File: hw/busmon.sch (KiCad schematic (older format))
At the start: 24 parts, among them J1 CONN_01X16, J3 DIL14, J4 DIL14, J5 DIL14, J6 DIL14, J7 CONN_01X02, J8 CONN_01X06, Q1 MMBT3906, Q2 MMBT3906, Q3 MMBT3906, Q4 MMBT3906, U1 ATMEGA164A-A

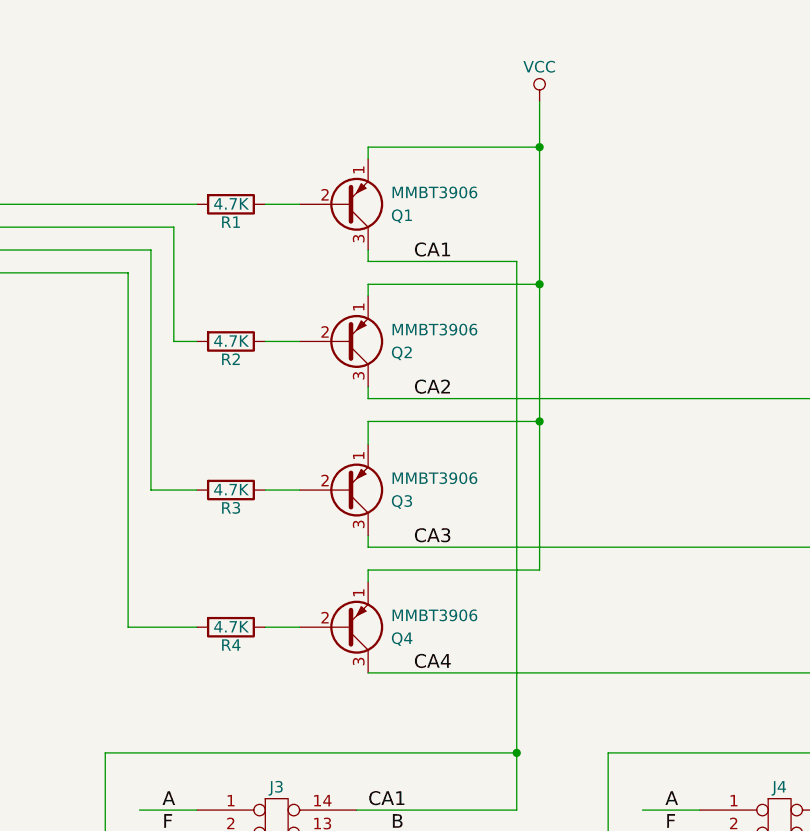
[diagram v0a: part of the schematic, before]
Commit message: use correct transistor pinout
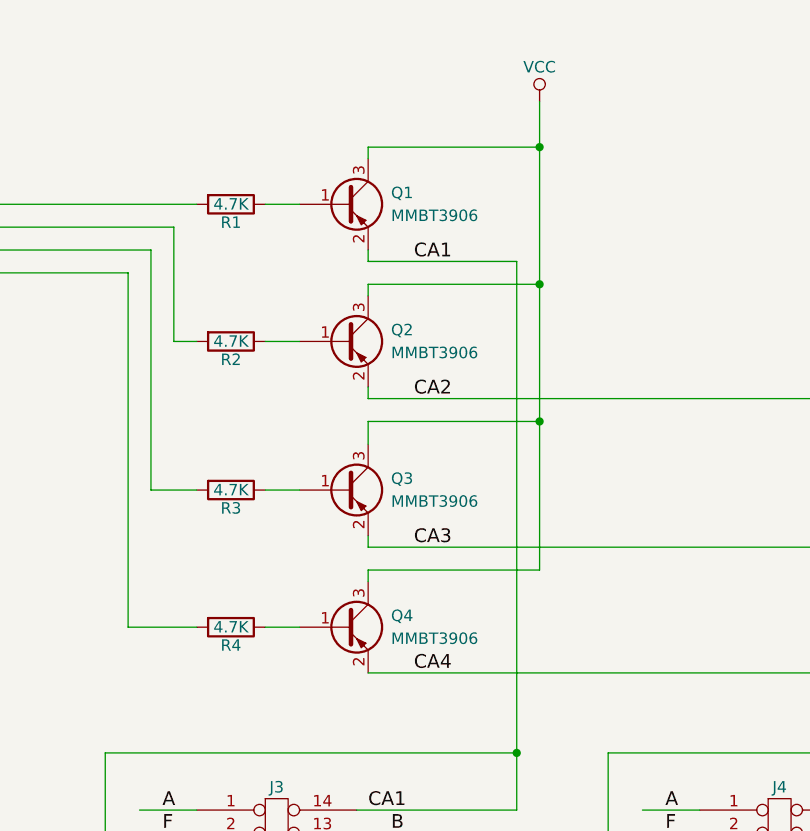
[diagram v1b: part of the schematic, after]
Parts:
- removed Q1, Q2, Q3, Q4: MMBT3906, TO_SOT_Packages_SMD:SOT-23, symbol Q_PNP_EBC
- added Q1, Q2, Q3, Q4: MMBT3906, symbol Q_PNP_BEC
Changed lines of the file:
@@
 CA2
-$Comp
-L Q_PNP_EBC Q1
-U 1 1 592DFC6D
-P 7950 3450
-F 0 "Q1" H 8150 3500 50  0000 L CNN
-F 1 "MMBT3906" H 8150 3400 50  0000 L CNN
-F 2 "TO_SOT_Packages_SMD:SOT-23" H 8150 3550 50  0001 C CNN
-F 3 "" H 7950 3450 50  0001 C CNN
-	1    7950 3450
-	1    0    0    1
-$EndComp
-$Comp
-L Q_PNP_EBC Q2
-U 1 1 592DFCA0
-P 7950 4050
-F 0 "Q2" H 8150 4100 50  0000 L CNN
-F 1 "MMBT3906" H 8150 4000 50  0000 L CNN
-F 2 "TO_SOT_Packages_SMD:SOT-23" H 8150 4150 50  0001 C CNN
-F 3 "" H 7950 4050 50  0001 C CNN
-	1    7950 4050
-	1    0    0    1
-$EndComp
 $Comp
 L VCC #PWR01
@@
 Entry Wire Line
 	4800 8850 4900 8950
-$Comp
-L Q_PNP_EBC Q3
-U 1 1 593E8971
-P 7950 4700
-F 0 "Q3" H 8150 4750 50  0000 L CNN
-F 1 "MMBT3906" H 8150 4650 50  0000 L CNN
-F 2 "TO_SOT_Packages_SMD:SOT-23" H 8150 4800 50  0001 C CNN
-F 3 "" H 7950 4700 50  0001 C CNN
-	1    7950 4700
-	1    0    0    1
-$EndComp
-$Comp
-L Q_PNP_EBC Q4
-U 1 1 593E89D1
-P 7950 5300
-F 0 "Q4" H 8150 5350 50  0000 L CNN
-F 1 "MMBT3906" H 8150 5250 50  0000 L CNN
-F 2 "TO_SOT_Packages_SMD:SOT-23" H 8150 5400 50  0001 C CNN
-F 3 "" H 7950 5300 50  0001 C CNN
-	1    7950 5300
-	1    0    0    1
-$EndComp
 Wire Wire Line
 	8050 4500 8050 4400
@@
 	1    0    0    -1
 $EndComp
+$Comp
+L Q_PNP_BEC Q1
+U 1 1 593ED485
+P 7950 3450
+F 0 "Q1" H 8150 3500 50  0000 L CNN
+F 1 "MMBT3906" H 8150 3400 50  0000 L CNN
+F 2 "" H 8150 3550 50  0001 C CNN
+F 3 "" H 7950 3450 50  0001 C CNN
+	1    7950 3450
+	1    0    0    -1
+$EndComp
+$Comp
+L Q_PNP_BEC Q2
+U 1 1 593ED62A
+P 7950 4050
+F 0 "Q2" H 8150 4100 50  0000 L CNN
+F 1 "MMBT3906" H 8150 4000 50  0000 L CNN
+F 2 "" H 8150 4150 50  0001 C CNN
+F 3 "" H 7950 4050 50  0001 C CNN
+	1    7950 4050
+	1    0    0    -1
+$EndComp
+$Comp
+L Q_PNP_BEC Q3
+U 1 1 593ED698
+P 7950 4700
+F 0 "Q3" H 8150 4750 50  0000 L CNN
+F 1 "MMBT3906" H 8150 4650 50  0000 L CNN
+F 2 "" H 8150 4800 50  0001 C CNN
+F 3 "" H 7950 4700 50  0001 C CNN
+	1    7950 4700
+	1    0    0    -1
+$EndComp
+$Comp
+L Q_PNP_BEC Q4
+U 1 1 593ED69E
+P 7950 5300
+F 0 "Q4" H 8150 5350 50  0000 L CNN
+F 1 "MMBT3906" H 8150 5250 50  0000 L CNN
+F 2 "" H 8150 5400 50  0001 C CNN
+F 3 "" H 7950 5300 50  0001 C CNN
+	1    7950 5300
+	1    0    0    -1
+$EndComp

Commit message: updated footprint associations
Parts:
- Q1, Q2, Q3, Q4: footprint (none) -> TO_SOT_Packages_SMD:SOT-23
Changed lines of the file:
@@
 F 0 "Q1" H 8150 3500 50  0000 L CNN
 F 1 "MMBT3906" H 8150 3400 50  0000 L CNN
-F 2 "" H 8150 3550 50  0001 C CNN
+F 2 "TO_SOT_Packages_SMD:SOT-23" H 8150 3550 50  0001 C CNN
 F 3 "" H 7950 3450 50  0001 C CNN
 	1    7950 3450
@@
 F 0 "Q2" H 8150 4100 50  0000 L CNN
 F 1 "MMBT3906" H 8150 4000 50  0000 L CNN
-F 2 "" H 8150 4150 50  0001 C CNN
+F 2 "TO_SOT_Packages_SMD:SOT-23" H 8150 4150 50  0001 C CNN
 F 3 "" H 7950 4050 50  0001 C CNN
 	1    7950 4050
@@
 F 0 "Q3" H 8150 4750 50  0000 L CNN
 F 1 "MMBT3906" H 8150 4650 50  0000 L CNN
-F 2 "" H 8150 4800 50  0001 C CNN
+F 2 "TO_SOT_Packages_SMD:SOT-23" H 8150 4800 50  0001 C CNN
 F 3 "" H 7950 4700 50  0001 C CNN
 	1    7950 4700
@@
 F 0 "Q4" H 8150 5350 50  0000 L CNN
 F 1 "MMBT3906" H 8150 5250 50  0000 L CNN
-F 2 "" H 8150 5400 50  0001 C CNN
+F 2 "TO_SOT_Packages_SMD:SOT-23" H 8150 5400 50  0001 C CNN
 F 3 "" H 7950 5300 50  0001 C CNN
 	1    7950 5300

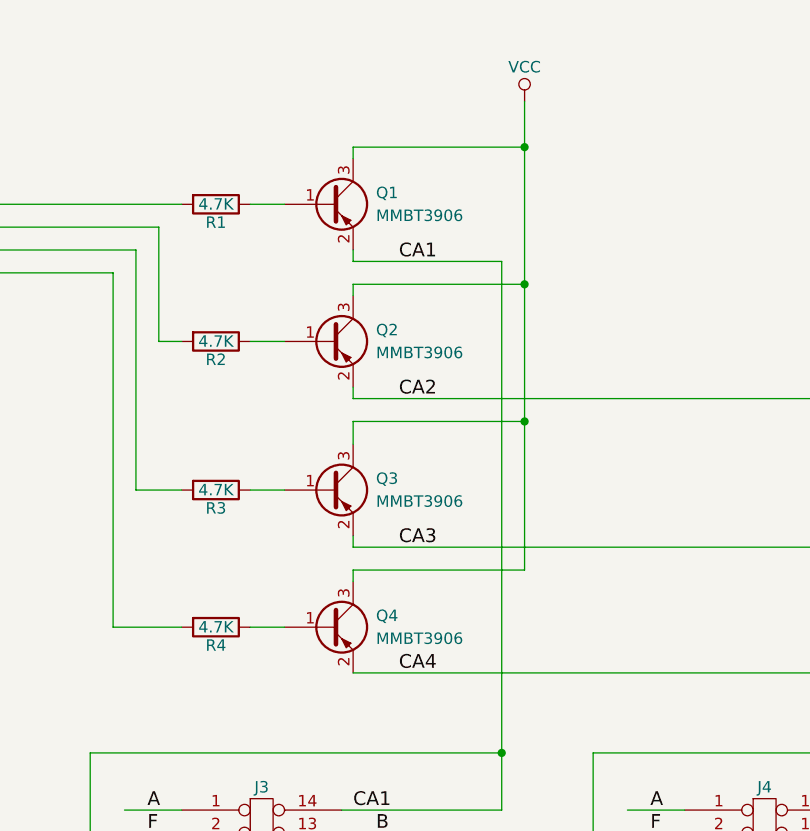
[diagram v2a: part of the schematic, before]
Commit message: fix transistor orientation
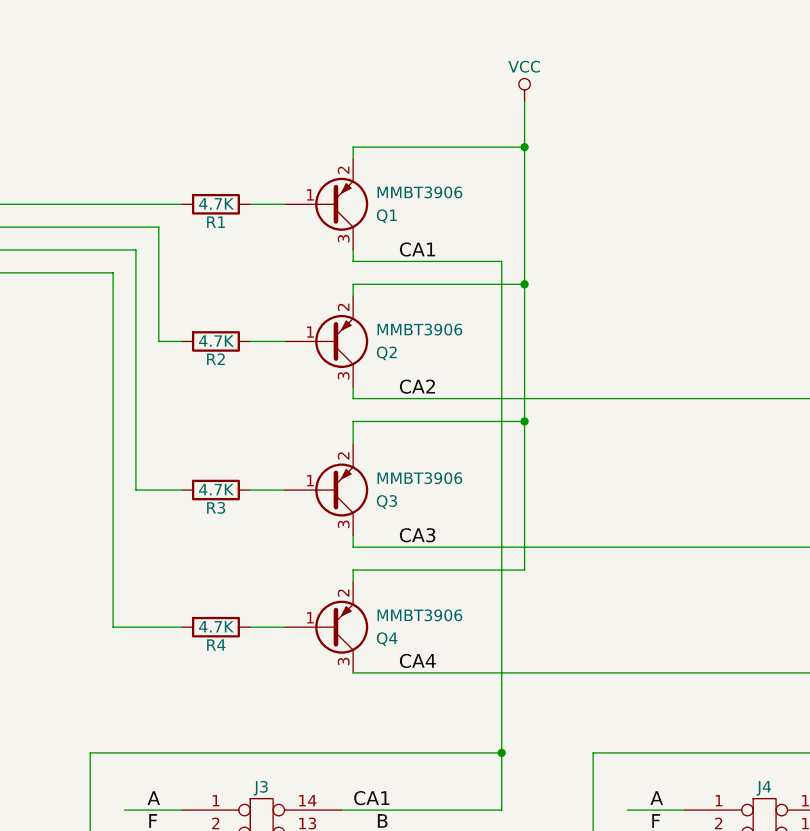
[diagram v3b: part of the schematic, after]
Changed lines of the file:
@@
 F 3 "" H 7950 3450 50  0001 C CNN
 	1    7950 3450
-	1    0    0    -1
+	1    0    0    1
 $EndComp
 $Comp
 L Q_PNP_BEC Q2
-U 1 1 593ED62A
+U 1 1 593EDF41
 P 7950 4050
 F 0 "Q2" H 8150 4100 50  0000 L CNN
@@
 F 3 "" H 7950 4050 50  0001 C CNN
 	1    7950 4050
-	1    0    0    -1
+	1    0    0    1
 $EndComp
 $Comp
 L Q_PNP_BEC Q3
-U 1 1 593ED698
+U 1 1 593EDFDF
 P 7950 4700
 F 0 "Q3" H 8150 4750 50  0000 L CNN
@@
 F 3 "" H 7950 4700 50  0001 C CNN
 	1    7950 4700
-	1    0    0    -1
+	1    0    0    1
 $EndComp
 $Comp
 L Q_PNP_BEC Q4
-U 1 1 593ED69E
+U 1 1 593EDFE5
 P 7950 5300
 F 0 "Q4" H 8150 5350 50  0000 L CNN
@@
 F 3 "" H 7950 5300 50  0001 C CNN
 	1    7950 5300
-	1    0    0    -1
+	1    0    0    1
 $EndComp
 $EndSCHEMATC

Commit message: converted project to KiCad 5
Hopefully the PCB is still good.
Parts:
- C1: symbol CP1 -> busmon-rescue:CP1
- J1: symbol CONN_01X16 -> busmon-rescue:CONN_01X16
- J3, J4, J5, J6: symbol DIL14 -> busmon-rescue:DIL14
- J7: symbol CONN_01X02 -> busmon-rescue:CONN_01X02
- J8: symbol CONN_01X06 -> busmon-rescue:CONN_01X06
- Q1, Q2, Q3, Q4: symbol Q_PNP_BEC -> busmon-rescue:Q_PNP_BEC
- R1, R10, R11, R2, R3, R4, R5, R6, R7, R8, R9: symbol R -> busmon-rescue:R
- U1: symbol ATMEGA164A-A -> busmon-rescue:ATMEGA164A-A
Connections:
- wire segments 192 -> 207
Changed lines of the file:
@@
-EESchema Schematic File Version 2
-LIBS:power
-LIBS:device
-LIBS:transistors
-LIBS:conn
-LIBS:linear
-LIBS:regul
-LIBS:74xx
-LIBS:cmos4000
-LIBS:adc-dac
-LIBS:memory
-LIBS:xilinx
-LIBS:microcontrollers
-LIBS:dsp
-LIBS:microchip
-LIBS:analog_switches
-LIBS:motorola
-LIBS:texas
-LIBS:intel
-LIBS:audio
-LIBS:interface
-LIBS:digital-audio
-LIBS:philips
-LIBS:display
-LIBS:cypress
-LIBS:siliconi
-LIBS:opto
-LIBS:atmel
-LIBS:contrib
-LIBS:valves
+EESchema Schematic File Version 4
 LIBS:busmon-cache
-EELAYER 25 0
+EELAYER 26 0
 EELAYER END
 $Descr A3 16535 11693
@@
 $EndDescr
 $Comp
-L DIL14 J3
+L busmon-rescue:DIL14 J3
 U 1 1 592DEE57
 P 7650 6400
@@
 B
 $Comp
-L DIL14 J4
+L busmon-rescue:DIL14 J4
 U 1 1 592DF5D1
 P 9850 6400
@@
 CA2
 $Comp
-L VCC #PWR01
+L busmon-rescue:VCC #PWR01
 U 1 1 592E0484
 P 8800 3000
@@
 CA2
 $Comp
-L R R5
+L busmon-rescue:R R5
 U 1 1 592E125C
 P 5300 2400
@@
 $EndComp
 $Comp
-L R R6
+L busmon-rescue:R R6
 U 1 1 592E12E2
 P 5300 2550
@@
 $EndComp
 $Comp
-L R R7
+L busmon-rescue:R R7
 U 1 1 592E13D9
 P 5300 2700
@@
 $EndComp
 $Comp
-L R R8
+L busmon-rescue:R R8
 U 1 1 592E13DF
 P 5300 2850
@@
 $EndComp
 $Comp
-L R R9
+L busmon-rescue:R R9
 U 1 1 592E14A8
 P 5300 3000
@@
 $EndComp
 $Comp
-L R R10
+L busmon-rescue:R R10
 U 1 1 592E14AE
 P 5300 3150
@@
 $EndComp
 $Comp
-L R R11
+L busmon-rescue:R R11
 U 1 1 592E14B4
 P 5300 3300
@@
 	8050 3200 8800 3200
 Wire Wire Line
-	8800 3000 8800 5050
+	8800 3000 8800 3200
 Wire Wire Line
 	8050 3850 8050 3800
@@
 	8050 4300 10650 4300
 Wire Wire Line
-	10650 4300 10650 6100
-Wire Wire Line
-	8700 3700 8700 6100
+	10650 4300 10650 5850
+Wire Wire Line
+	8700 3700 8700 5850
 Wire Wire Line
 	6900 6300 6900 5850
@@
 MAN3620\nright high digit
 $Comp
-L VCC #PWR02
+L busmon-rescue:VCC #PWR02
 U 1 1 592E23BD
 P 3200 2000
@@
 $EndComp
 $Comp
-L GND #PWR03
+L busmon-rescue:GND #PWR03
 U 1 1 592E23F1
 P 3150 6450
@@
 16 bit hexadecimal bus monitor
 $Comp
-L CONN_01X02 J7
+L busmon-rescue:CONN_01X02 J7
 U 1 1 592E2D34
 P 3350 8500
@@
 	3000 8450 3150 8450
 Wire Wire Line
-	3000 8250 3000 8450
+	3000 8250 3000 8300
 Wire Wire Line
 	3150 8550 3000 8550
 Wire Wire Line
-	3000 8550 3000 8750
-$Comp
-L VCC #PWR04
+	3000 8550 3000 8700
+$Comp
+L busmon-rescue:VCC #PWR04
 U 1 1 592E2EB4
 P 3000 8250
@@
 $EndComp
 $Comp
-L GND #PWR05
+L busmon-rescue:GND #PWR05
 U 1 1 592E2EEA
 P 3000 8750
@@
 low data input
 $Comp
-L ATMEGA164A-A U1
+L busmon-rescue:ATMEGA164A-A U1
 U 1 1 593E6C60
 P 3300 4250
@@
 $EndComp
 $Comp
-L DIL14 J5
+L busmon-rescue:DIL14 J5
 U 1 1 593E7114
 P 11850 6400
@@
 	12200 6700 12450 6700
 $Comp
-L DIL14 J6
+L busmon-rescue:DIL14 J6
 U 1 1 593E71EE
 P 13900 6400
@@
 	3000 6250 3000 6350
 Wire Wire Line
-	3000 6350 3300 6350
+	3000 6350 3100 6350
 Wire Wire Line
 	3150 6350 3150 6450
@@
 	3000 2250 3000 2100
 Wire Wire Line
-	3000 2100 3400 2100
-Wire Wire Line
-	3200 2000 3200 2250
+	3000 2100 3100 2100
+Wire Wire Line
+	3200 2000 3200 2100
 Wire Wire Line
 	3100 2250 3100 2100
@@
 	1750 3750 1750 3550
 $Comp
-L VCC #PWR06
+L busmon-rescue:VCC #PWR06
 U 1 1 593EAAB8
 P 1750 3550
@@
 Text Label 4500 5050 0    60   ~ 0
 D15
-Wire Bus Line
-	4800 4450 4800 8850
 Entry Wire Line
 	4700 4350 4800 4450
@@
 Connection ~ 8800 4400
 $Comp
-L R R1
+L busmon-rescue:R R1
 U 1 1 593E9A49
 P 7450 3450
@@
 $EndComp
 $Comp
-L R R2
+L busmon-rescue:R R2
 U 1 1 593E9AF1
 P 7450 4050
@@
 $EndComp
 $Comp
-L R R3
+L busmon-rescue:R R3
 U 1 1 593E9BED
 P 7450 4700
@@
 $EndComp
 $Comp
-L R R4
+L busmon-rescue:R R4
 U 1 1 593E9BF3
 P 7450 5300
@@
 	8050 4950 12650 4950
 Wire Wire Line
-	12650 4950 12650 6100
+	12650 4950 12650 5850
 Wire Wire Line
 	12650 6100 12200 6100
@@
 	8050 5500 14750 5500
 Wire Wire Line
-	14750 5500 14750 6100
+	14750 5500 14750 5850
 Wire Wire Line
 	14750 6100 14250 6100
@@
 CA4
 $Comp
-L CP1 C1
+L busmon-rescue:CP1 C1
 U 1 1 593EE2FE
 P 2700 8500
@@
 decoupling\ncap
 $Comp
-L CONN_01X06 J8
+L busmon-rescue:CONN_01X06 J8
 U 1 1 593EF856
 P 6100 4600
@@
 	5450 4350 5450 5100
 $Comp
-L GND #PWR07
+L busmon-rescue:GND #PWR07
 U 1 1 593F01FF
 P 5450 5100
@@
 	5750 4450 5750 4200
 $Comp
-L VCC #PWR08
+L busmon-rescue:VCC #PWR08
 U 1 1 593F0381
 P 5750 4200
@@
 programming\nheader
 $Comp
-L CONN_01X16 J1
+L busmon-rescue:CONN_01X16 J1
 U 1 1 593ECF2F
 P 5550 8200
@@
 $EndComp
 $Comp
-L Q_PNP_BEC Q1
+L busmon-rescue:Q_PNP_BEC Q1
 U 1 1 593ED485
 P 7950 3450
@@
 $EndComp
 $Comp
-L Q_PNP_BEC Q2
+L busmon-rescue:Q_PNP_BEC Q2
 U 1 1 593EDF41
 P 7950 4050
@@
 $EndComp
 $Comp
-L Q_PNP_BEC Q3
+L busmon-rescue:Q_PNP_BEC Q3
 U 1 1 593EDFDF
 P 7950 4700
@@
 $EndComp
 $Comp
-L Q_PNP_BEC Q4
+L busmon-rescue:Q_PNP_BEC Q4
 U 1 1 593EDFE5
 P 7950 5300
@@
 	1    0    0    1
 $EndComp
+Wire Wire Line
+	8800 3200 8800 3800
+Wire Wire Line
+	8700 5850 8700 6100
+Wire Wire Line
+	10650 5850 10650 6100
+Wire Wire Line
+	3150 6350 3200 6350
+Wire Wire Line
+	3100 6350 3150 6350
+Wire Wire Line
+	3200 6350 3300 6350
+Wire Wire Line
+	3100 2100 3200 2100
+Wire Wire Line
+	3200 2100 3200 2250
+Wire Wire Line
+	3200 2100 3400 2100
+Wire Wire Line
+	8800 3800 8800 4400
+Wire Wire Line
+	8800 4400 8800 5050
+Wire Wire Line
+	12650 5850 12650 6100
+Wire Wire Line
+	14750 5850 14750 6100
+Wire Wire Line
+	3000 8300 3000 8450
+Wire Wire Line
+	3000 8700 3000 8750
+Wire Bus Line
+	4800 4450 4800 8850
 $EndSCHEMATC

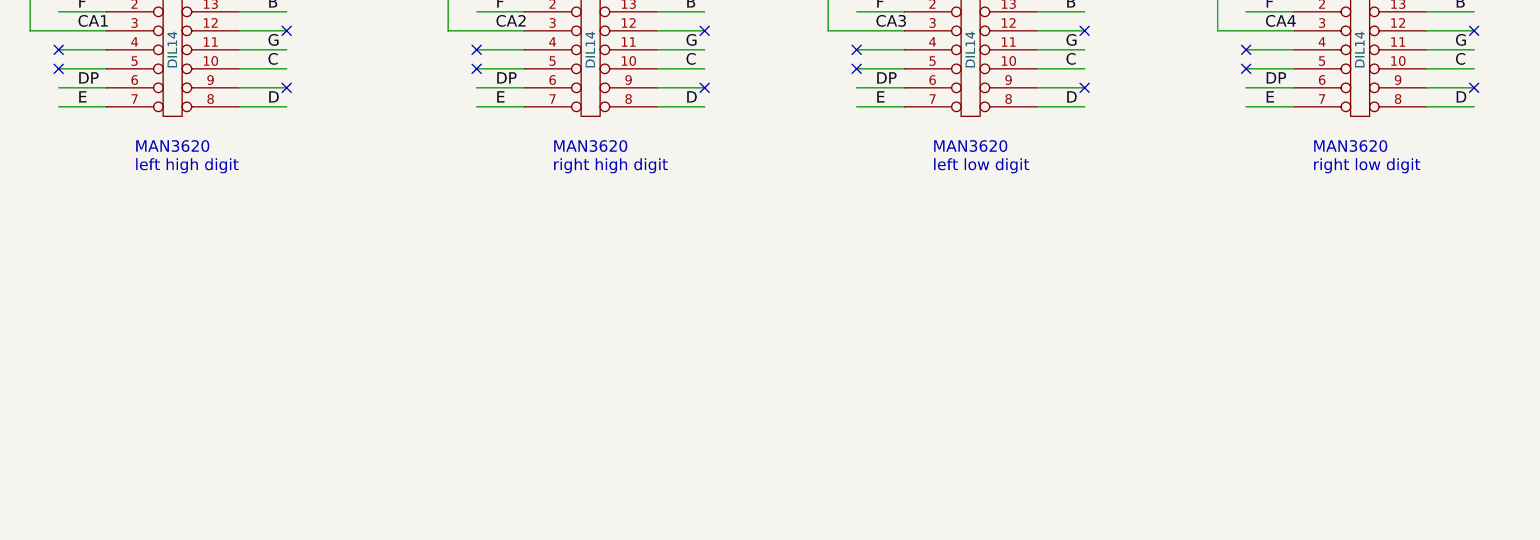
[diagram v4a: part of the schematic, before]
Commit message: improve schematic, minor silkscreen fixes
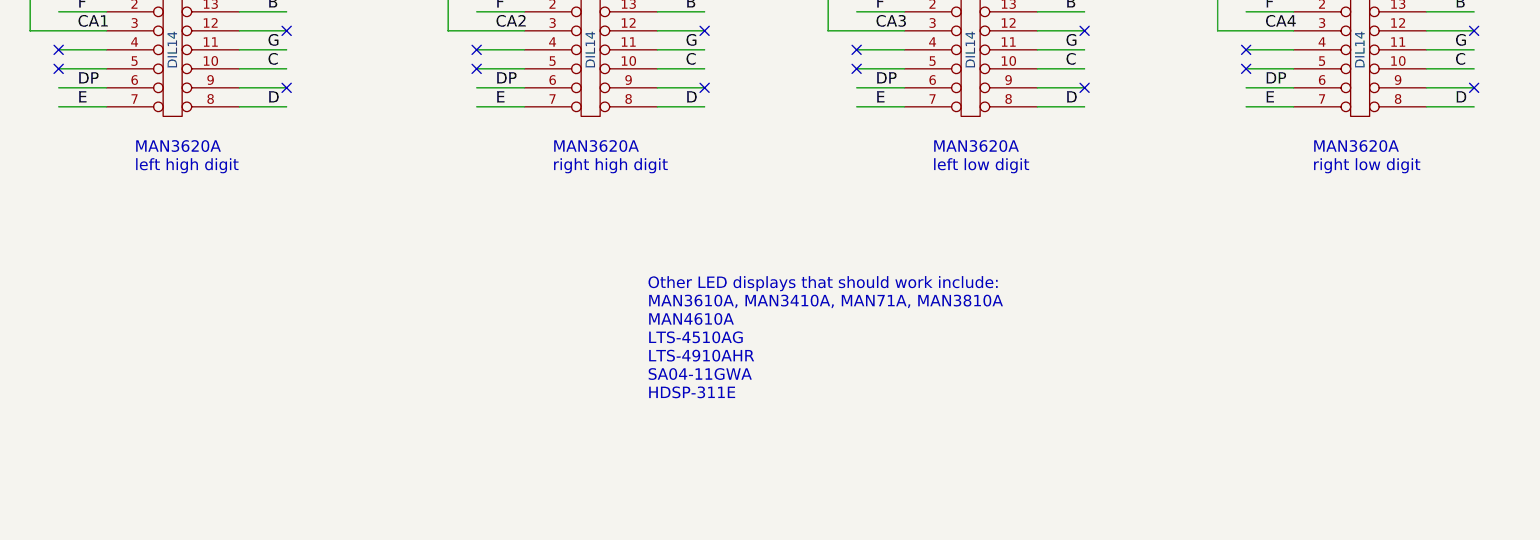
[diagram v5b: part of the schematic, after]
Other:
- note added: "MAN3620A\nleft high digit"
- note added: "MAN3620A\nleft low digit"
- note added: "MAN3620A\nright high digit"
- note added: "MAN3620A\nright low digit"
- note added: "Other LED displays that should work include:\nMAN3610A, MAN3410A, MAN71A, MAN3810A\nMAN4610A\nLTS-4510AG\nLTS-4910AHR\nSA04-11GWA\nHDSP-311E"
- note removed: "MAN3620\nleft high digit"
- note removed: "MAN3620\nleft low digit"
- note removed: "MAN3620\nright high digit"
- note removed: "MAN3620\nright low digit"
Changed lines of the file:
@@
 G
 Text Notes 7450 7050 0    60   ~ 0
-MAN3620\nleft high digit
+MAN3620A\nleft high digit
 Text Notes 9650 7050 0    60   ~ 0
-MAN3620\nright high digit
+MAN3620A\nright high digit
 $Comp
 L busmon-rescue:VCC #PWR02
@@
 	14250 6700 14500 6700
 Text Notes 11650 7050 0    60   ~ 0
-MAN3620\nleft low digit
+MAN3620A\nleft low digit
 Text Notes 13650 7050 0    60   ~ 0
-MAN3620\nright low digit
+MAN3620A\nright low digit
 Wire Wire Line
 	3000 6250 3000 6350
@@
 Wire Bus Line
 	4800 4450 4800 8850
+Text Notes 10150 8250 0    60   ~ 0
+Other LED displays that should work include:\nMAN3610A, MAN3410A, MAN71A, MAN3810A\nMAN4610A\nLTS-4510AG\nLTS-4910AHR\nSA04-11GWA\nHDSP-311E
 $EndSCHEMATC

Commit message: get ready to make public
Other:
- note added: "16 bit hexadecimal bus monitor\nCopyright (c) 2017-2019, David H. Hovemeyer <david.hovemeyer@gmail.com>\nMade available under terms of CERN Open Hardware License v1.2\nSee README.md"
- note removed: "16 bit hexadecimal bus monitor"
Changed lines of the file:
@@
 	1    0    0    -1
 $EndComp
-Text Notes 11950 10200 0    60   ~ 0
-16 bit hexadecimal bus monitor
+Text Notes 11900 10400 0    60   ~ 0
+16 bit hexadecimal bus monitor\nCopyright (c) 2017-2019, David H. Hovemeyer <david.hovemeyer@gmail.com>\nMade available under terms of CERN Open Hardware License v1.2\nSee README.md
 $Comp
 L busmon-rescue:CONN_01X02 J7
@@
 Wire Wire Line
 	3000 8700 3000 8750
+Text Notes 10150 8250 0    60   ~ 0
+Other LED displays that should work include:\nMAN3610A, MAN3410A, MAN71A, MAN3810A\nMAN4610A\nLTS-4510AG\nLTS-4910AHR\nSA04-11GWA\nHDSP-311E
 Wire Bus Line
 	4800 4450 4800 8850
-Text Notes 10150 8250 0    60   ~ 0
-Other LED displays that should work include:\nMAN3610A, MAN3410A, MAN71A, MAN3810A\nMAN4610A\nLTS-4510AG\nLTS-4910AHR\nSA04-11GWA\nHDSP-311E
 $EndSCHEMATC
